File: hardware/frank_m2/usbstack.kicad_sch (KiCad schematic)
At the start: 7 parts, among them J15 SS-52100-004

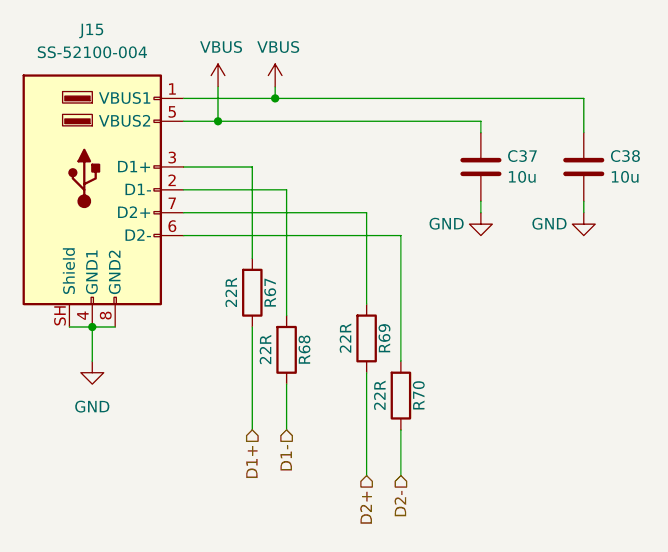
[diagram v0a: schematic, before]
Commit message: Move hardware/frank_m2 to frank-lab repo, restore v2.06 from master
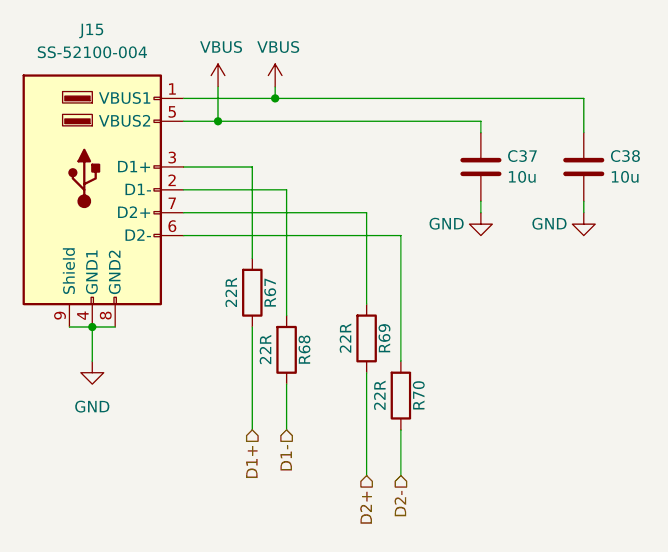
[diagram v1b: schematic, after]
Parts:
- J15: footprint FRANK:USB_A_Stacked -> FRANK:USB Type A (stacked); symbol FRANK:USB_A_Stacked -> Connector:USB_A_Stacked
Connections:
- net GND: now also J15.9 (Shield); no longer J15.SH (Shield)

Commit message: Rename and localize hardware/frank_m2 footprints, 3D models
- Removed 5 unused footprints, 1 unused 3D model
- Renamed 28 footprints to KiCad standard naming
- Renamed 30 3D models, normalized all to .step
- Copied 12 system 3D models (KiCad built-in) to local 3d/ dir
- Replaced all ${KICADx_3DMODEL_DIR} refs with ${KIPRJMOD}/3d/
- Fixed wrong library prefixes (LIBS:, DC-005-5A-2.0:, etc.)
- Project is now fully self-contained (no external 3D model dependencies)
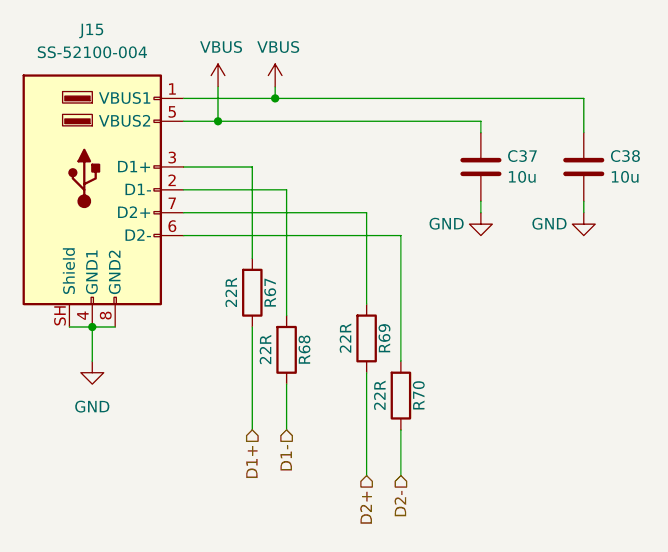
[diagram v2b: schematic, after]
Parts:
- J15: footprint FRANK:USB Type A (stacked) -> FRANK:USB_A_Stacked
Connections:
- net GND: now also J15.SH (Shield); no longer J15.9 (Shield)

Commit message: Make hardware/frank_m2 fully self-contained
- Extracted 16 symbols from KiCad global libraries into FRANK.kicad_sym
  (LM358, NCP1117, Conn_01x03_Pin, USB_A_Stacked, SW_Push, etc.)
- Merged 3 standalone symbol files into FRANK.kicad_sym, removed originals
- Updated all lib_id references from global (Device:, Connector:, etc.) to FRANK:
- Cleaned sym-lib-table to single FRANK entry
- Project now has zero external library dependencies
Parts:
- J15: symbol Connector:USB_A_Stacked -> FRANK:USB_A_Stacked
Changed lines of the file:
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@@
 	)
 	(symbol
-		(lib_id "Connector:USB_A_Stacked")
+		(lib_id "FRANK:USB_A_Stacked")
 		(at 121.92 86.36 0)
 		(unit 1)
